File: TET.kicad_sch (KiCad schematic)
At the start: 67 parts, among them J1 SWT, M1 MountingHole, M2 MountingHole, M3 MountingHole, M4 MountingHole, U1 E80-900M2213S_C42464134, U10 TLV75533PDBVR, U11 INA226AIDGSR, U12 TCAN330GDCNR, U13 SMA_1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

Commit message: ✨ feat(schematic): start connections for STM32L4
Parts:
- removed D1, D2, D3: SS14, Diode_SMD:D_SMA, symbol Device:D_Schottky_Small
- removed H1, H2: PC/104 Connector, Connector_PinSocket_2.54mm:PinSocket_2x26_P2.54mm_Vertical, symbol Connector_Generic:Conn_02x26_Odd_Even
- removed NT1, NT2: NetTie_2, symbol Device:NetTie_2
- removed R2, R3: 10k, Resistor_SMD:R_0603_1608Metric, symbol Device:R_Small
- removed U10: TLV75533PDBVR, TET-Footprints:SOT-23-5_L3.0-W1.7-P0.95-LS2.8-BR, symbol TET-Symbols:TLV75533PDBVR
- removed U11: INA226AIDGSR, TET-Footprints:MSOP-10_L3.0-W3.0-P0.50-LS5.0-BL, symbol TET-Symbols:INA226AIDGSR
- added C16, C17, C18, C19: 100nF, Capacitor_SMD:C_0603_1608Metric, symbol Device:C_Small
- added C20: 10uF, Capacitor_SMD:C_0603_1608Metric, symbol Device:C_Small
- added C21: 10nF, Capacitor_SMD:C_0603_1608Metric, symbol Device:C_Small
- added C22, C23: 1uF, Capacitor_SMD:C_0603_1608Metric, symbol Device:C_Small
- added FB1: 120R, Inductor_SMD:L_0603_1608Metric, symbol Device:FerriteBead_Small
- C1: value 22uF -> 100nF
- C2: value 22uF -> 20pF
- C3: value 0.1uF -> 20pF
- R1: value 0.1 -> 10k; footprint Resistor_SMD:R_0603_1608Metric -> (none)
- U15: value X50328MSB2GI -> 8 MHz
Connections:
- net SENSE+ is gone; now on net GND: R1.1
- net SENSE- is gone; now on net BOOT0: R1.2
- net +3.3V: now also U2.1 (VBAT), U2.24 (VDD), U2.36 (VDD), U2.48 (VDD), C16.1, C17.1, C18.1, C19.1, C20.1, C23.1, FB1.2; no longer C1.1, C3.1
- net GND: now also U2.23 (VSS), U2.35 (VSS), U2.47 (VSS), U2.8 (VSSA/VREF-), C16.2, C17.2, C18.2, C19.2, C20.2, C21.2, C22.2, C23.2
- net SCL0: no longer U2.11 (PA1)
- net SDA0: no longer U2.12 (PA2)
- net SWCLK: now also U2.37 (PA14(JTCKSWCLK))
- net SWDIO: now also U2.34 (PA13(JTMSSWDIO)
- net BOOT0: now reaches U2.44 (PH3/BOOT0)
- net OSC_IN: now reaches U2.5 (PH0-OSC_IN(PH0))
- net OSC_IN: now also C2.1, U15.2 (OSC2)
- net OSC_OUT: now reaches U2.6 (PH1-OSC_OUT(PH1))
- net OSC_OUT: now also C3.1, U15.1 (OSC1)
- net NRST: now reaches U2.7 (NRST)
- net NRST: now also C1.1
- net +3.3VA: now reaches U2.9 (VDDA/VREF+)
- net +3.3VA: now also C21.1, C22.1, FB1.1
- no-connect marks 33 -> 2
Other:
- added sheet Power_Supply (TET-Power-Supply.kicad_sch)
- note added: "CL = 2*(CL0-Cs) = 2*(20pF-10pF) = 20pF"
- note removed: "5 V enters from the EPS (PWR_4-6), passes through a current/voltage monitor (INA226), and is regulated to 3.3 V by an LDO (TLV755)."
- moved on the sheet: C10, C11, C12, C13, C14, C15, C8, C9, D4, D5, D6, J1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

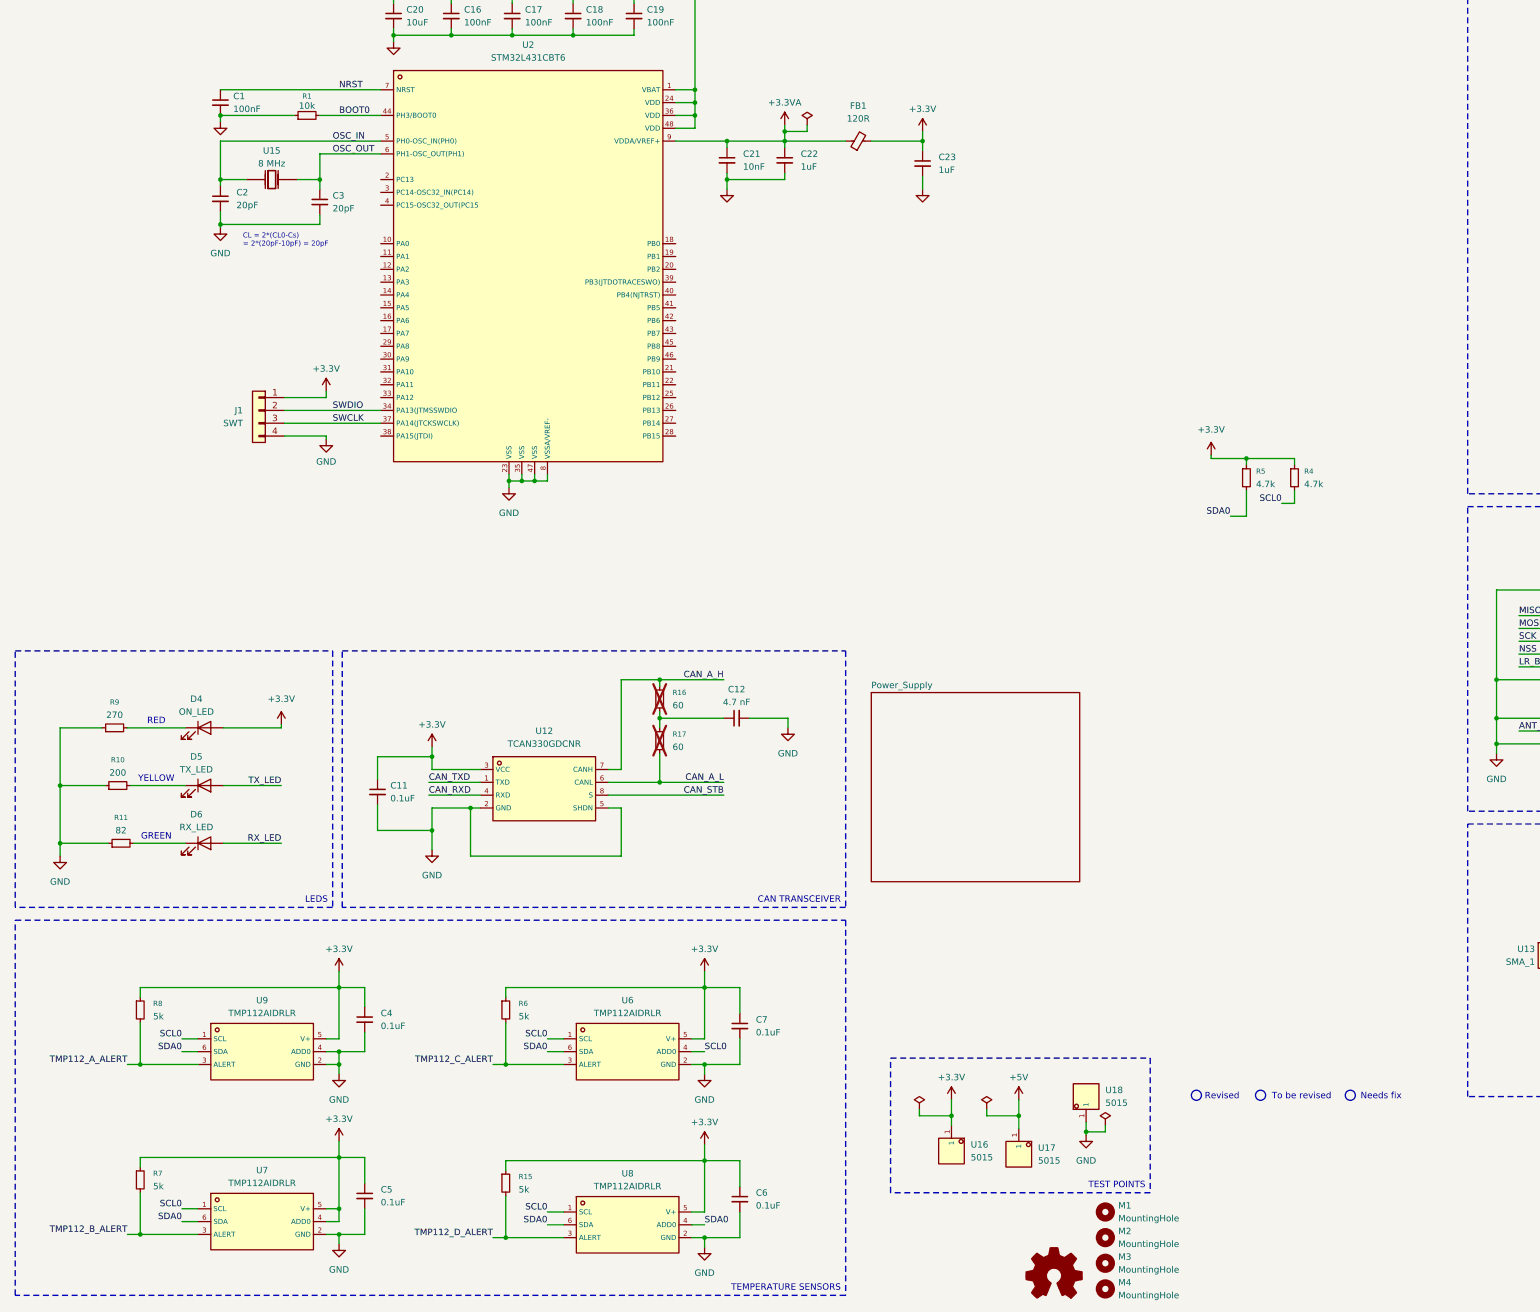
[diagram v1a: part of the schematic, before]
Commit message: ✨ feat(schematic): add pinout STM32
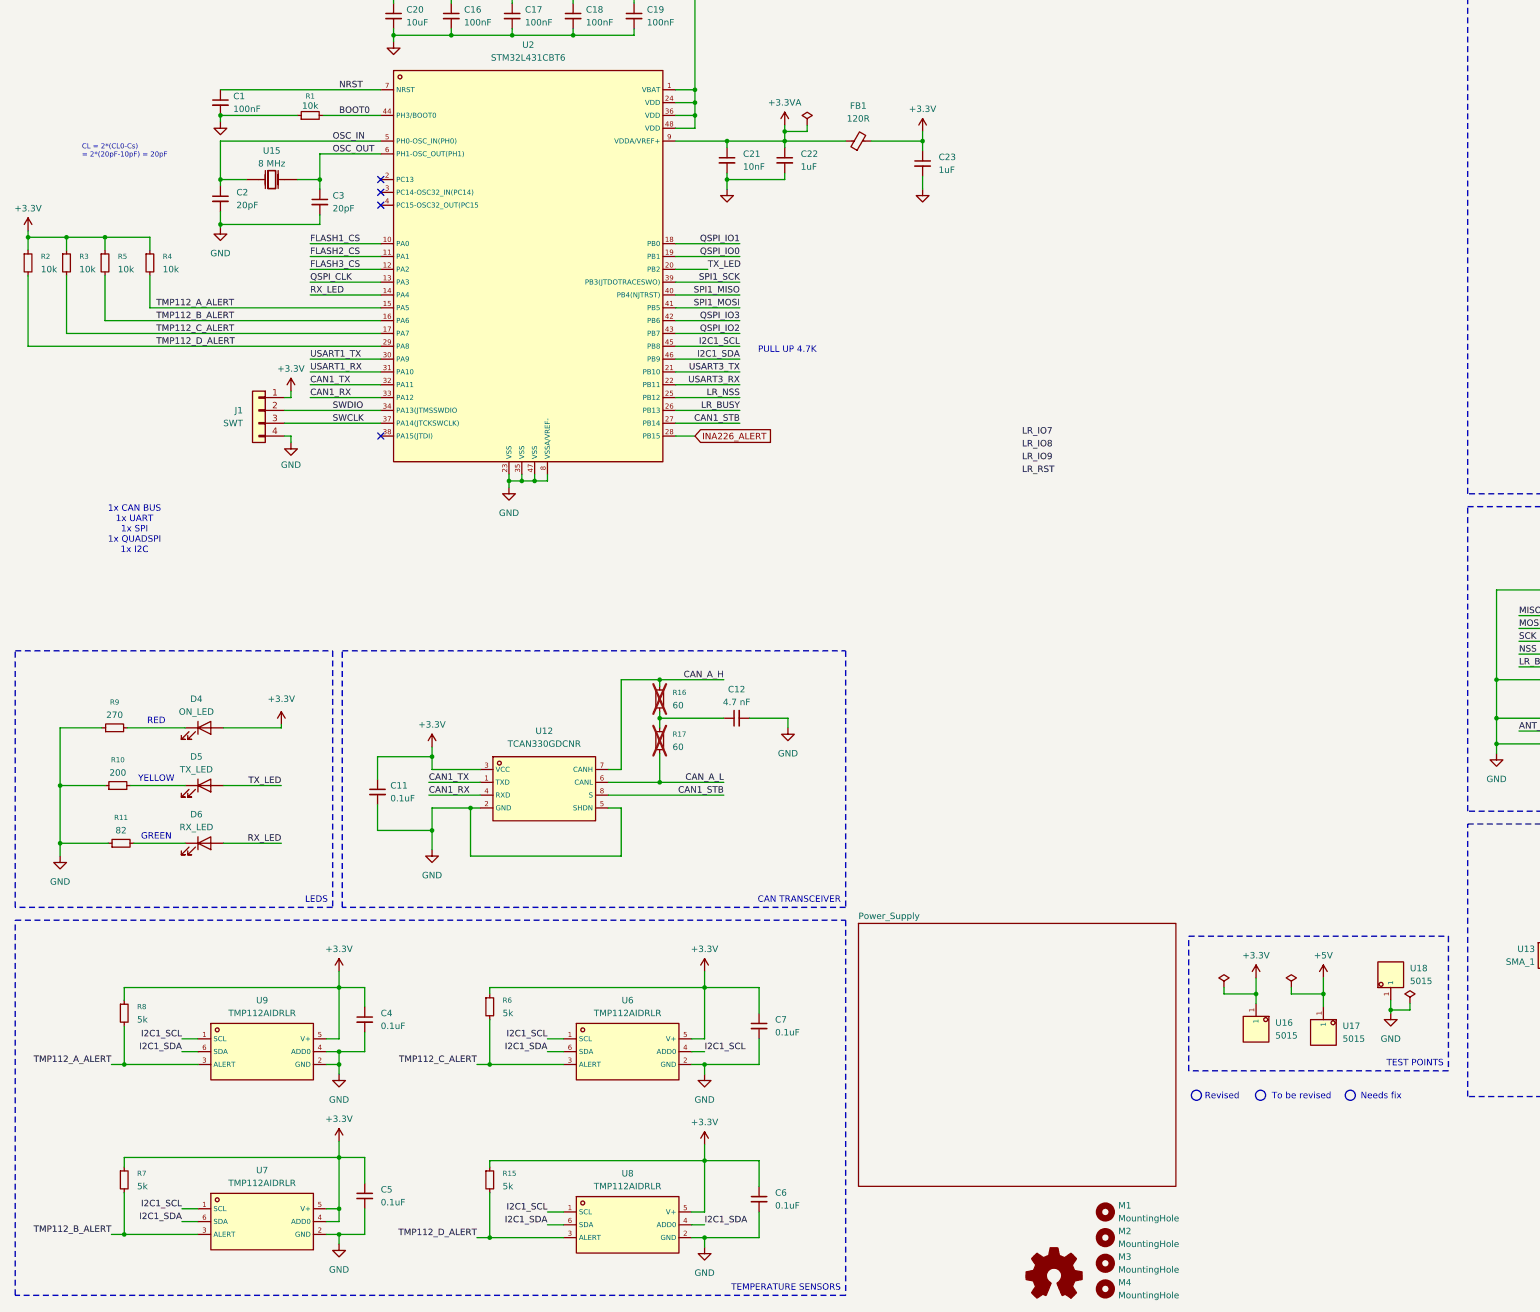
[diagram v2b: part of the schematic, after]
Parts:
- added R2, R3: 10k, symbol Device:R_Small
- R4, R5: value 4.7k -> 10k; footprint Resistor_SMD:R_0603_1608Metric -> (none)
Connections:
- net CAN_RXD is gone; now on net CAN1_RX: U12.4 (RXD)
- net CAN_STB is gone; now on net CAN1_STB: U12.8 (S)
- net CAN_TXD is gone; now on net CAN1_TX: U12.1 (TXD)
- net +3.3V: now also R2.1, R3.1
- net FLASH1_CS: now also U2.10 (PA0)
- net FLASH2_CS: now also U2.11 (PA1)
- net FLASH3_CS: now also U2.12 (PA2)
- net LR_BUSY: now also U2.26 (PB13)
- net QSPI_CLK: now also U2.13 (PA3)
- net QSPI_IO0: now also U2.19 (PB1)
- net QSPI_IO1: now also U2.18 (PB0)
- net QSPI_IO2: now also U2.43 (PB7)
- net QSPI_IO3: now also U2.42 (PB6)
- net RX_LED: now also U2.14 (PA4)
- net TMP112_A_ALERT: now also R4.2, U2.15 (PA5)
- net TMP112_B_ALERT: now also R5.2, U2.16 (PA6)
- net TMP112_C_ALERT: now also U2.17 (PA7), R3.2
- net TMP112_D_ALERT: now also U2.29 (PA8), R2.2
- net TX_LED: now also U2.20 (PB2)
- net USART3_TX: now reaches U2.21 (PB10)
- net USART3_RX: now reaches U2.22 (PB11)
- net LR_NSS: now reaches U2.25 (PB12)
- net CAN1_STB: now reaches U2.27 (PB14)
- net INA226_ALERT: now reaches U2.28 (PB15)
- net USART1_TX: now reaches U2.30 (PA9)
- net USART1_RX: now reaches U2.31 (PA10)
- net CAN1_TX: now reaches U2.32 (PA11)
- net CAN1_RX: now reaches U2.33 (PA12)
- net SPI1_SCK: now reaches U2.39 (PB3(JTDOTRACESWO))
- net SPI1_MISO: now reaches U2.40 (PB4(NJTRST))
- net SPI1_MOSI: now reaches U2.41 (PB5)
- net I2C1_SCL: now reaches U2.45 (PB8)
- net I2C1_SCL: now also U6.1 (SCL), U6.4 (ADD0), U7.1 (SCL), U8.1 (SCL), U9.1 (SCL)
- net I2C1_SDA: now reaches U2.46 (PB9)
- net I2C1_SDA: now also U6.6 (SDA), U7.6 (SDA), U8.4 (ADD0), U8.6 (SDA), U9.6 (SDA)
- removed net SCL0: R4.2, U6.1 (SCL), U6.4 (ADD0), U7.1 (SCL), U8.1 (SCL), U9.1 (SCL)
- removed net SDA0: R5.2, U6.6 (SDA), U7.6 (SDA), U8.4 (ADD0), U8.6 (SDA), U9.6 (SDA)
- no-connect marks 2 -> 6
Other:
- note added: "1x CAN BUS 1x UART 1x SPI 1x QUADSPI 1x I2C"
- note added: "PULL UP 4.7K"
- moved on the sheet: C6, C7, R1, R15, R6, R7, R8, U16, U17, U18

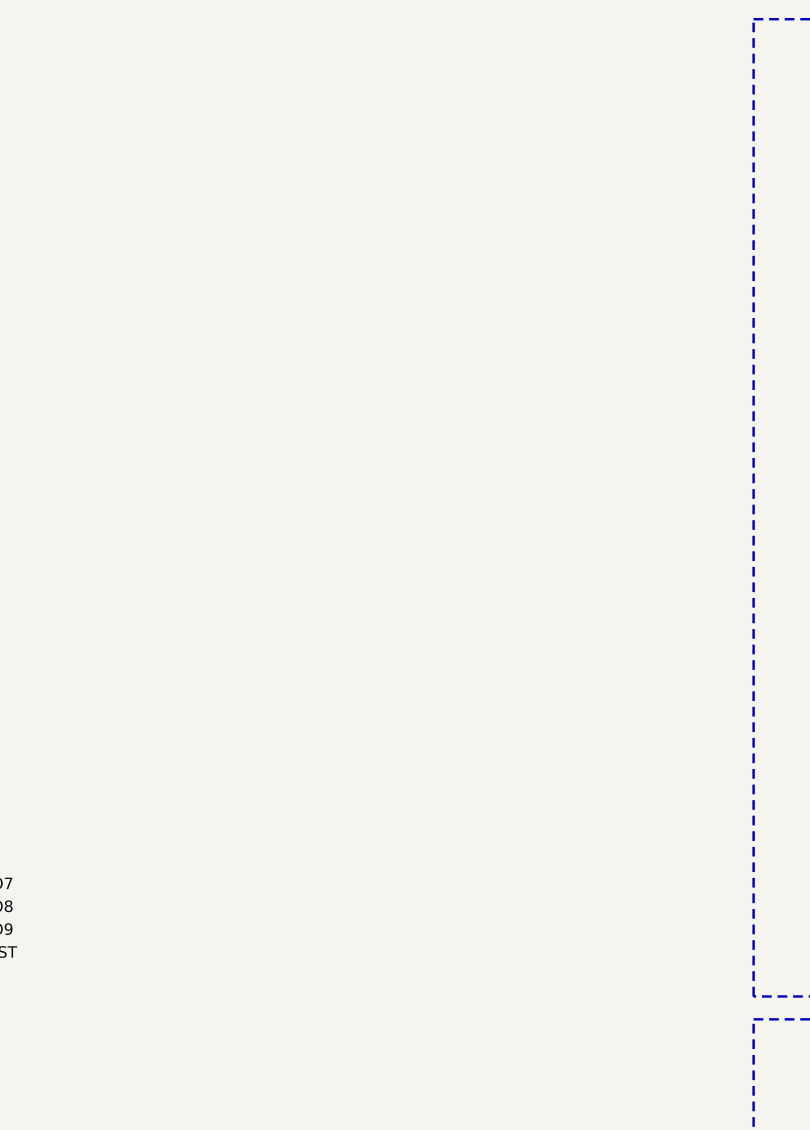
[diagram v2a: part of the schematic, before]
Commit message: ♻️ ref(schematic): change MCU from 48 pins to 64 pins
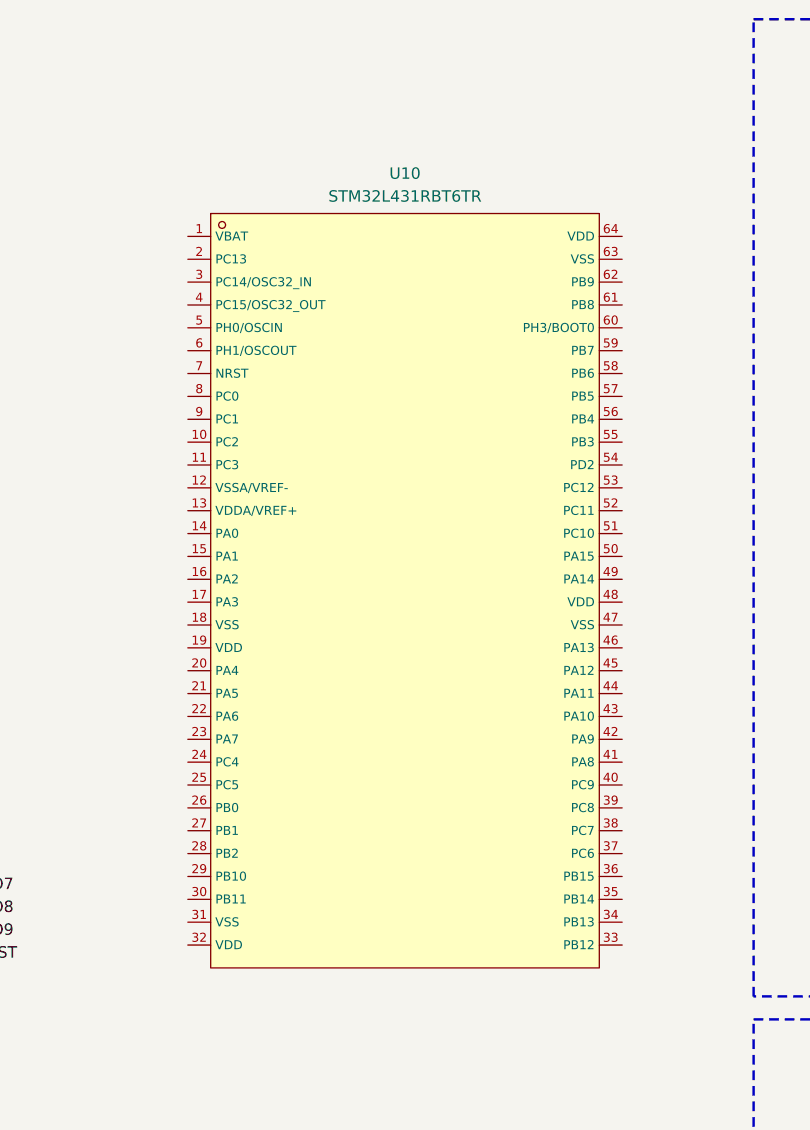
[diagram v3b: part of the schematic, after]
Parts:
- added U10: STM32L431RBT6TR, TET-Footprints:LQFP-64_L10.0-W10.0-P0.50-LS12.0-BL, symbol TET-Symbols:STM32L431RBT6TR
